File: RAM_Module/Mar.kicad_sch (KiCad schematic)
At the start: 8 parts, among them SW2 SW_DIP_x04, SW3 SW_SPDT, U1 74LS173, U2 74LS157

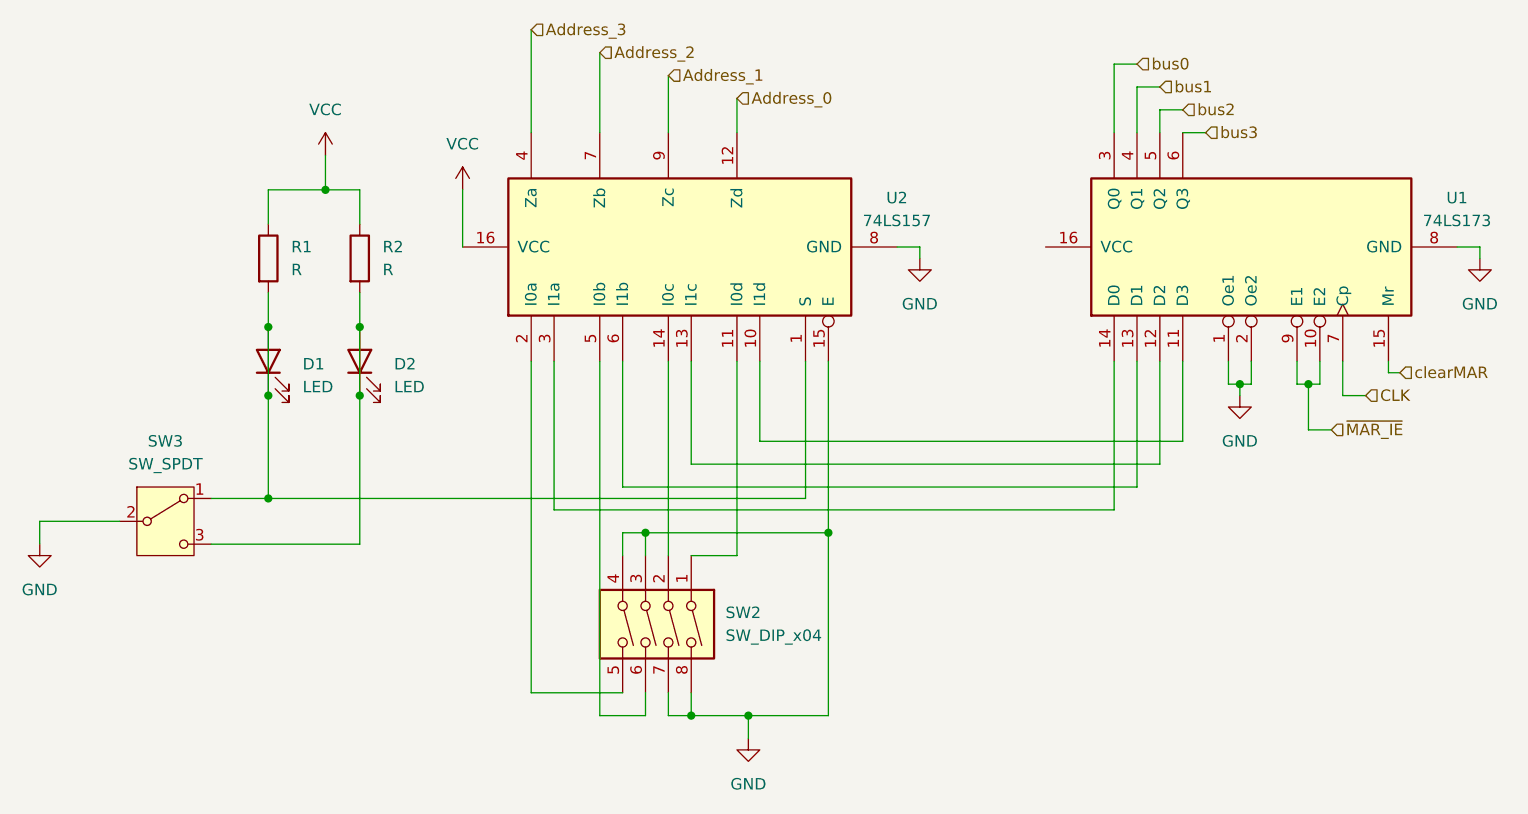
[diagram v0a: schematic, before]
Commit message: added buses for addresses. RAM WIP
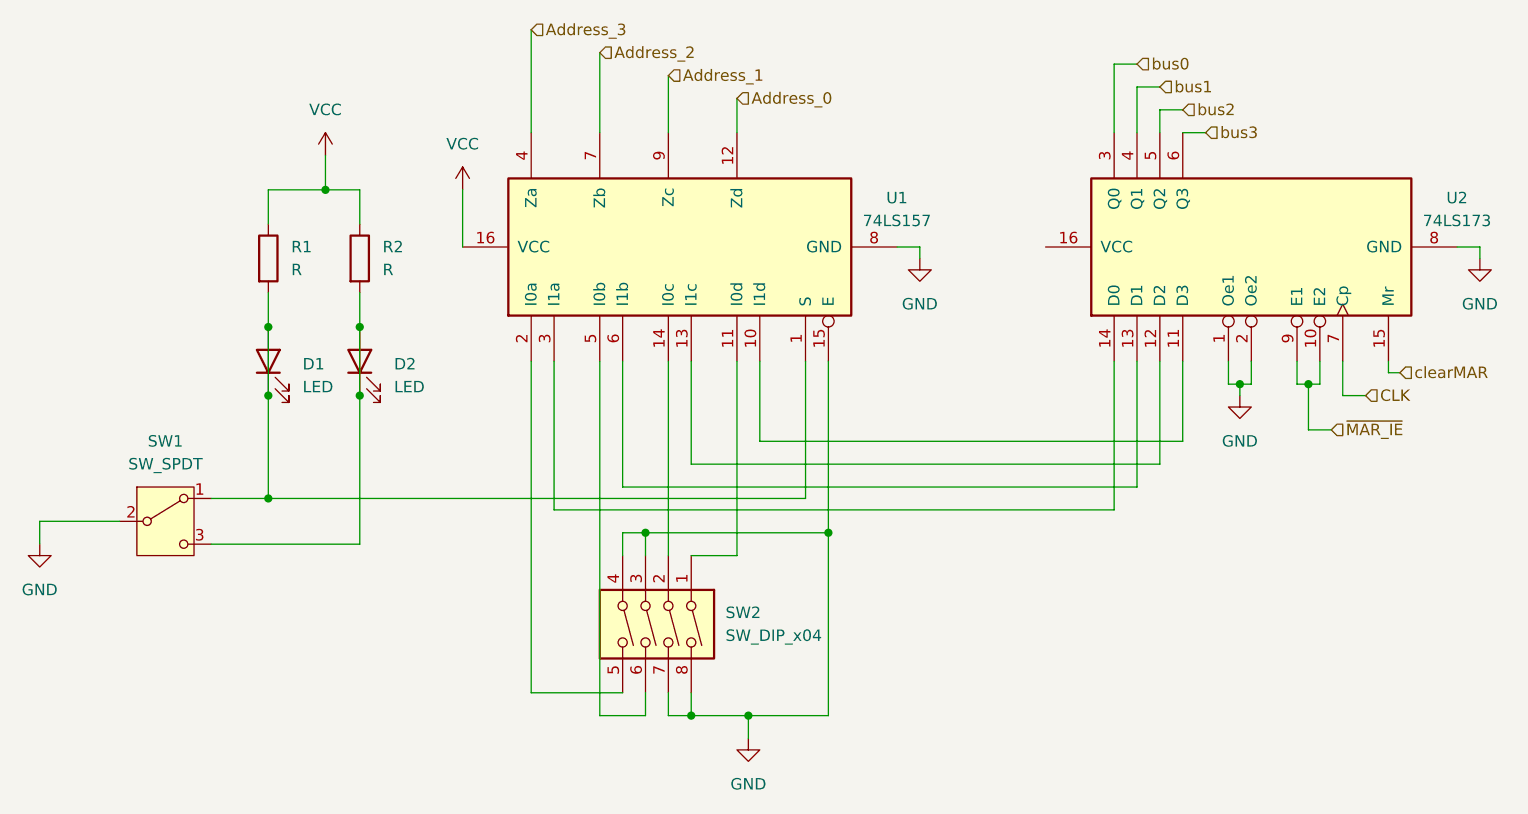
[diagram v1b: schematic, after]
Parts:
- renumbered SW3 to SW1, U2 to U1, U1 to U2
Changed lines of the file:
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@@
 		(dnp no)
 		(fields_autoplaced yes)
-		(property "Reference" "U1"
+		(property "Reference" "U2"
 			(at 231.14 85.9946 90)
 			(effects
@@
 			(project "RAM_Module"
 				(path "/03b00b70-3754-4eac-a53e-5e31c1a5687c/6c0a268e-8373-4fc4-b910-175fae74551a"
-					(reference "U1")
+					(reference "U2")
 					(unit 1)
 				)
@@
 		(dnp no)
 		(fields_autoplaced yes)
-		(property "Reference" "SW3"
+		(property "Reference" "SW1"
 			(at 87.63 113.03 0)
 			(effects
@@
 			(project ""
 				(path "/03b00b70-3754-4eac-a53e-5e31c1a5687c/6c0a268e-8373-4fc4-b910-175fae74551a"
-					(reference "SW3")
+					(reference "SW1")
 					(unit 1)
 				)
@@
 		(dnp no)
 		(fields_autoplaced yes)
-		(property "Reference" "#PWR09"
+		(property "Reference" "#PWR04"
 			(at 105.41 85.09 0)
 			(effects
@@
 			(project ""
 				(path "/03b00b70-3754-4eac-a53e-5e31c1a5687c/6c0a268e-8373-4fc4-b910-175fae74551a"
-					(reference "#PWR09")
+					(reference "#PWR04")
 					(unit 1)
 				)
@@
 		(dnp no)
 		(fields_autoplaced yes)
-		(property "Reference" "#PWR04"
+		(property "Reference" "#PWR08"
 			(at 207.01 114.3 0)
 			(effects
@@
 			(project ""
 				(path "/03b00b70-3754-4eac-a53e-5e31c1a5687c/6c0a268e-8373-4fc4-b910-175fae74551a"
-					(reference "#PWR04")
+					(reference "#PWR08")
 					(unit 1)
 				)
@@
 		(dnp no)
 		(fields_autoplaced yes)
-		(property "Reference" "#PWR08"
+		(property "Reference" "#PWR03"
 			(at 73.66 130.81 0)
 			(effects
@@
 			(project "RAM_Module"
 				(path "/03b00b70-3754-4eac-a53e-5e31c1a5687c/6c0a268e-8373-4fc4-b910-175fae74551a"
-					(reference "#PWR08")
+					(reference "#PWR03")
 					(unit 1)
 				)
@@
 		(dnp no)
 		(fields_autoplaced yes)
-		(property "Reference" "#PWR05"
+		(property "Reference" "#PWR09"
 			(at 233.68 99.06 0)
 			(effects
@@
 			(project "RAM_Module"
 				(path "/03b00b70-3754-4eac-a53e-5e31c1a5687c/6c0a268e-8373-4fc4-b910-175fae74551a"
-					(reference "#PWR05")
+					(reference "#PWR09")
 					(unit 1)
 				)
@@
 		(dnp no)
 		(fields_autoplaced yes)
-		(property "Reference" "#PWR010"
+		(property "Reference" "#PWR05"
 			(at 120.65 88.9 0)
 			(effects
@@
 			(project "RAM_Module"
 				(path "/03b00b70-3754-4eac-a53e-5e31c1a5687c/6c0a268e-8373-4fc4-b910-175fae74551a"
-					(reference "#PWR010")
+					(reference "#PWR05")
 					(unit 1)
 				)
@@
 		(dnp no)
 		(fields_autoplaced yes)
-		(property "Reference" "U2"
+		(property "Reference" "U1"
 			(at 168.91 85.9946 90)
 			(effects
@@
 			)
 		)
-		(property "Datasheet" "http://www.ti.com/lit/gpn/sn74LS157"
+		(property "Datasheet" "https://www.jameco.com/Jameco/Products/ProdDS/301612-DS01.pdf"
 			(at 143.51 91.44 0)
 			(effects
@@
 			(project "RAM_Module"
 				(path "/03b00b70-3754-4eac-a53e-5e31c1a5687c/6c0a268e-8373-4fc4-b910-175fae74551a"
-					(reference "U2")
-					(unit 1)
-				)
+					(reference "U1")
+					(unit 1)
+				)

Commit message: fixed Ram register, fixed mar in ram.v, updated caps in alu, ram, and instruction register
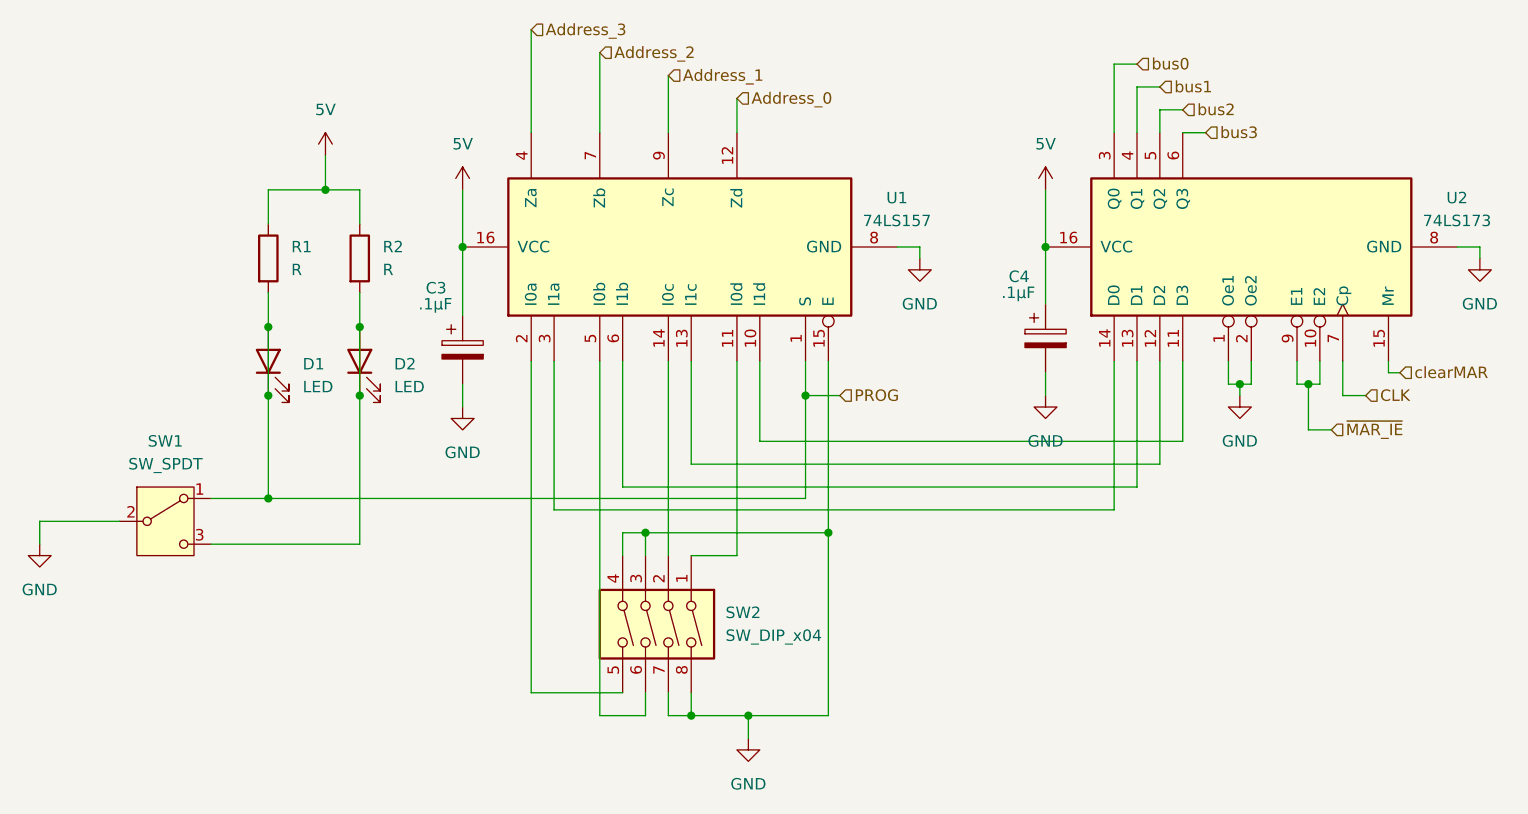
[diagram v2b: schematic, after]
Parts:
- added C3, C4: .1µF, symbol Device:C_Polarized
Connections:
- net VCC is gone; now on net 5V: R1.1, R2.1, U1.16 (VCC)
- net GND: now also C3.2, C4.2
- net 5V: now reaches U2.16 (VCC)
- net 5V: now also C3.1, C4.1
- net PROG: now reaches D1.1 (K), D1.2 (A), R1.2, SW1.1 (A), U1.1 (S)

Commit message: Added Program Counter Schematic
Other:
- company: (none) -> Arsenal Gear
- title: (none) -> Ram Module
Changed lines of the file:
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@@
 	(generator_version "9.0")
 	(paper "A4")
+	(title_block
+		(title "Ram Module")
+		(date "2025-08-25")
+		(company "Arsenal Gear")
+	)
 	(junction
 		(at 109.22 107.95)
